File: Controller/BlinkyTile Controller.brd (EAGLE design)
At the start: 35 x 25 mm, 28 parts, among them CON1 USB_MICROSMT+THRUHULE, CON2 F-2X04-DIL-100, Q1 CRYSTAL_4PAD2520, SW1 SPST_TACT-EVQQ2, SW2 SPST_TACT-EVQQ2, U1 MK20D--VFM5, U2 W25Q80BV, U3 74LVC1G17DCK, U4 74LVC1G17DCK, U5 74LVC1G17DCK

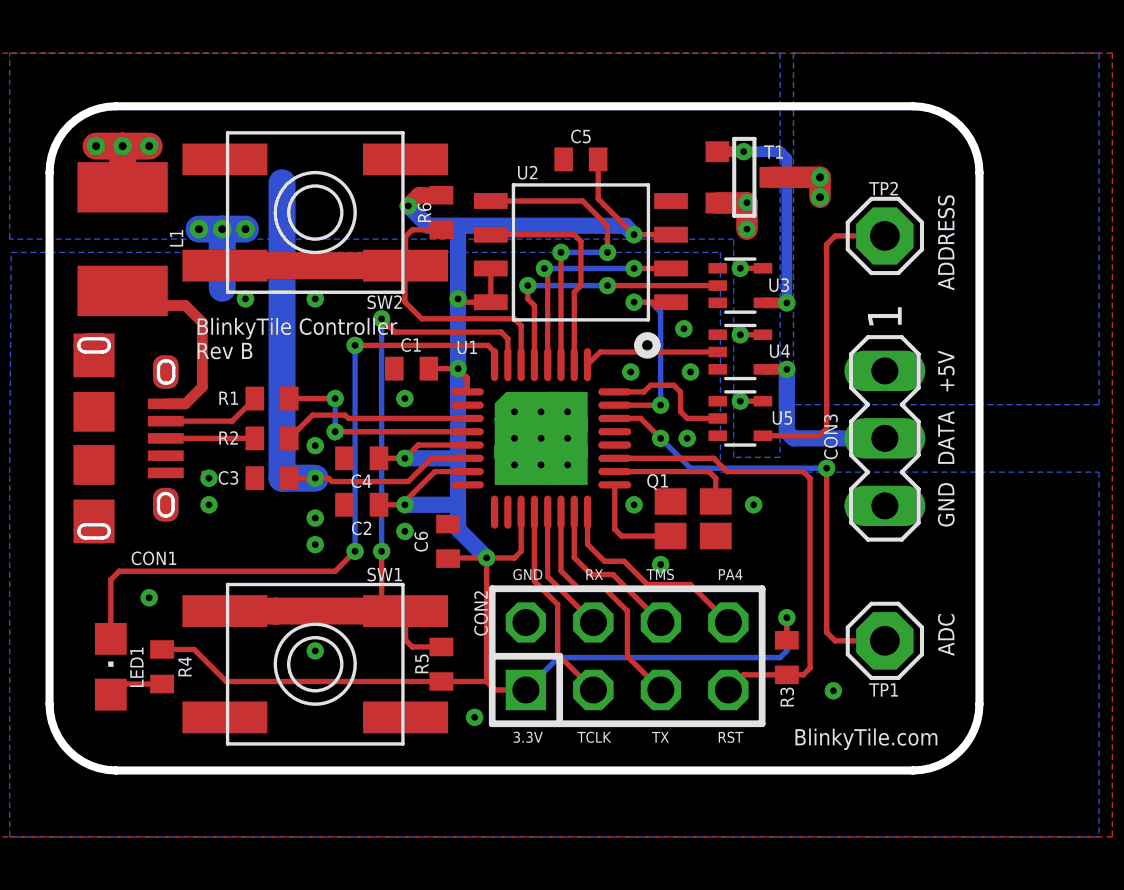
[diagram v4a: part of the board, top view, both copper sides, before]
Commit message: PCB updates: Drop pullup resistors, change connector
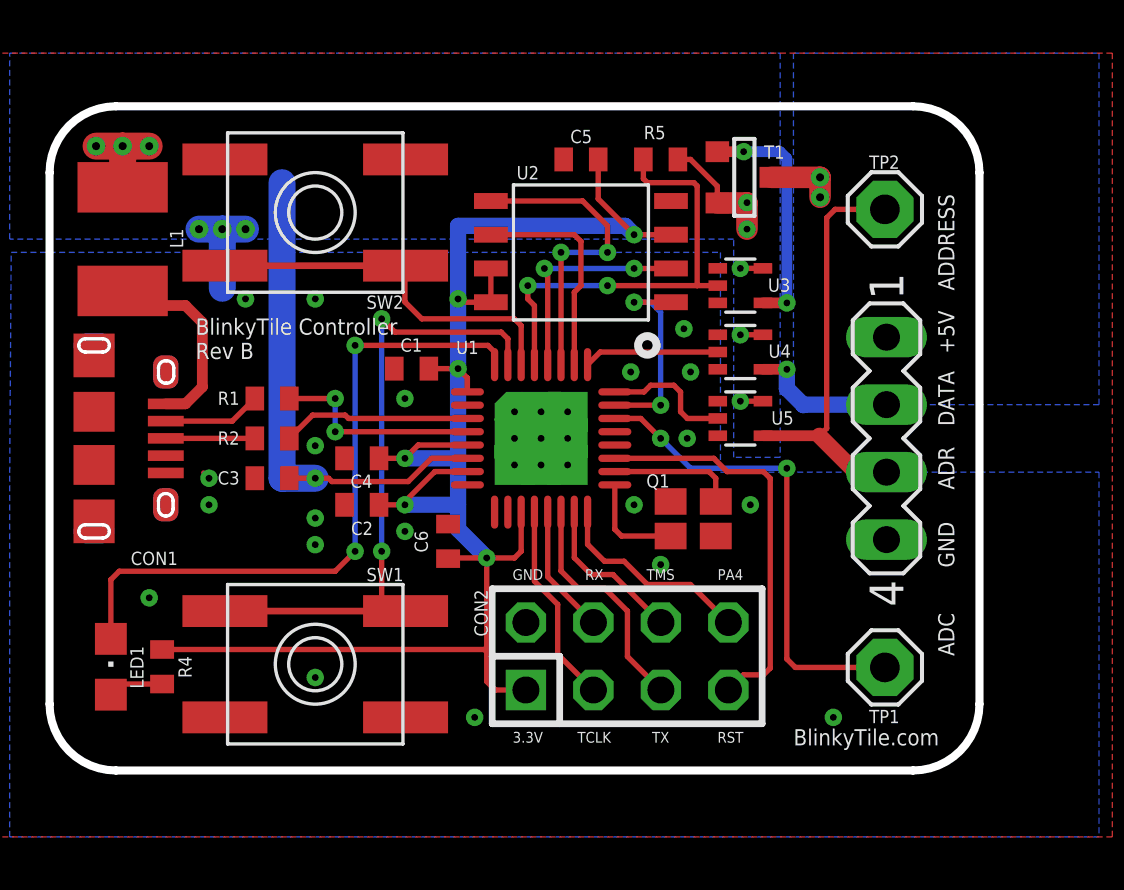
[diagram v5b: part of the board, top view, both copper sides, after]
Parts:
- removed CON3: (no value), con-lstb:MA03-1
- removed R3: 1k, adafruit:R0402
- removed R6: 10k, adafruit:R0402
- added SV1: (no value), con-lstb:MA04-1
- R4: value 1k -> 330
- R5: value 10k -> 1k
- moved R5 20.7 mm to (23.0, 10.5), turned to 0 degrees
- moved TP1 1.00 mm to (31.4, -8.62)
- moved TP2 1.00 mm to (31.4, 8.62)
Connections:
- net +3V3: no longer R3.2, R5.2, R6.2
- net +5V: now also R5.2
- net GND: now also SV1.4; no longer CON3.3
- net LED_DATA: now also SV1.2; no longer CON3.2
- net N$4: now also SV1.3
- net N$5: now also SV1.1; no longer CON3.1
- net POWER_ENABLE: now also R5.1
- net RESET: no longer R3.1
- net SW1: no longer R5.1
- net SW2: no longer R6.1
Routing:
- net +3V3: track 80.2 -> 63.6 mm, vias 8 -> 6
- net POWER_ENABLE: track 10.2 -> 16.8 mm
- net N$4: track 11.8 -> 15.9 mm
- net SW1: track 27.1 -> 23.8 mm
- net RESET: track 18.2 -> 15.2 mm
- net SW2: track 17.0 -> 14.4 mm
- net +5V: track 27.7 -> 30.2 mm
- net LED_DATA: track 7.04 -> 5.64 mm
- net ADC15: track 17.3 -> 18.3 mm
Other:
- board text added: "ADR"

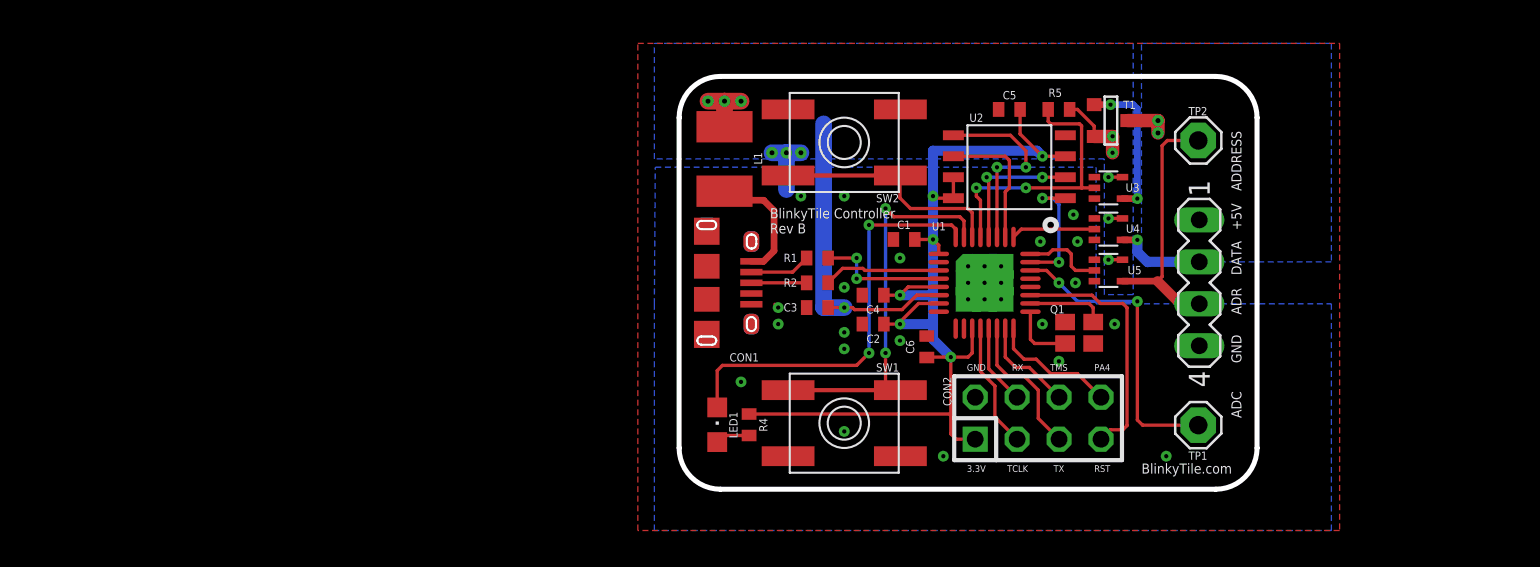
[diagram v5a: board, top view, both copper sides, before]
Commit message: Updated controller and panel designs
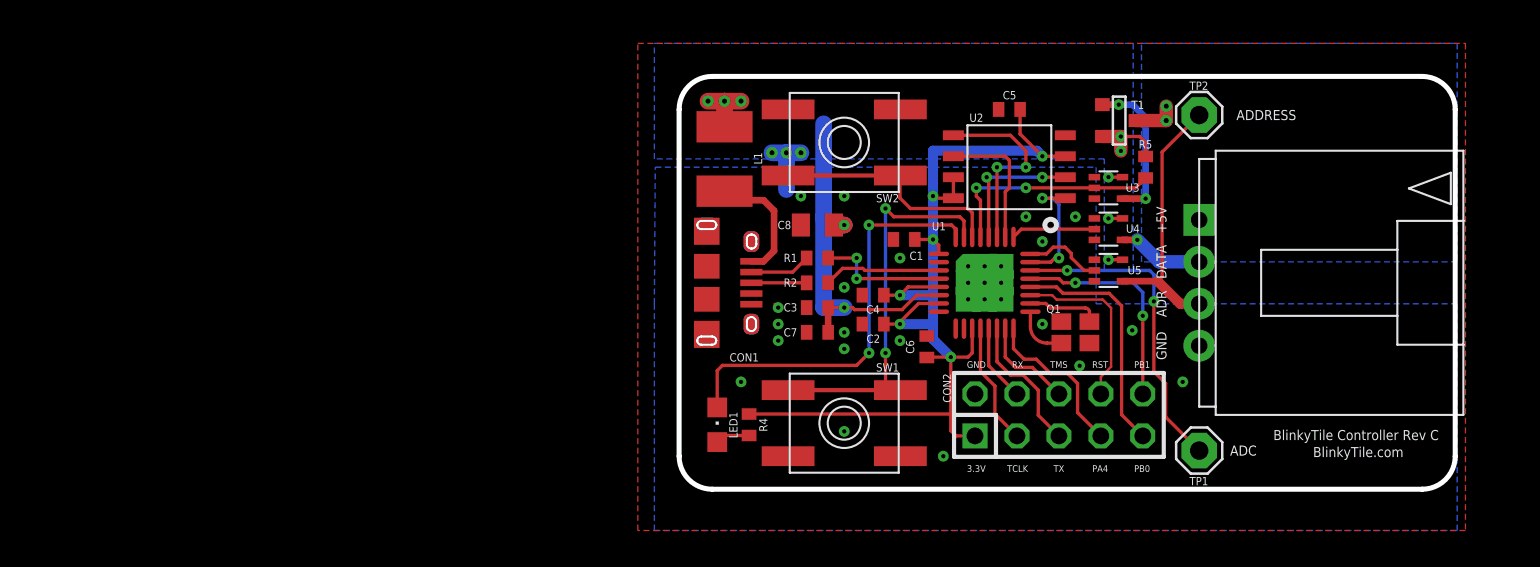
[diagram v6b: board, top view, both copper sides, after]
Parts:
- added C7: 100nF, adafruit:C0402
- added C8: 10uF, adafruit:C0805K
- CON2: value F-2X04-DIL-100 -> F-2X05-DIL-100; device con-headers-jp:DIL-100-2X04 -> con-headers-jp:DIL-100-2X05
- SV1: device con-lstb:MA04-1 -> dodocohedreled:4-PIN_DUPONT
- moved R5 6.31 mm to (28.2, 7.00), turned to 90 degrees
- moved TP1 1.54 mm to (31.5, -10.2)
- moved TP2 1.54 mm to (31.5, 10.2)
- moved CON2 1.28 mm to (23.0, -8.00)
- moved T1 0.50 mm to (26.6, 9.80)
- moved Q1 0.23 mm to (24.0, -3.00)
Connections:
- new net PB0: CON2.9, U1.20
- new net PB1: CON2.10, U1.21
- net +5V: now also C7.1, C8.1
- net GND: now also C7.2, C8.2, SV1.P$4; no longer SV1.4
- net LED_DATA: now also SV1.P$2; no longer SV1.2
- net N$4: now also SV1.P$3; no longer SV1.3
- net N$5: now also SV1.P$1; no longer SV1.1
- net PA4: now also CON2.7; no longer CON2.8
- net RESET: now also CON2.8; no longer CON2.7
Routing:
- net PB0: track 0.00 -> 14.4 mm
- net PB1: track 0.00 -> 13.3 mm, vias 0 -> 2
- net RESET: track 15.2 -> 10.7 mm
- net +5V: track 30.2 -> 33.7 mm, vias 9 -> 10
- net POWER_ENABLE: track 16.8 -> 13.6 mm
- net PA4: track 7.73 -> 9.73 mm
- net ADC15: track 18.3 -> 19.4 mm
- net N$2: track 3.88 -> 3.19 mm
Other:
- board size 35 x 25 mm -> 47 x 25 mm
- board text added: "BlinkyTile Controller Rev C"
- board text added: "PB0"
- board text added: "PB1"
- board text removed: "BlinkyTile Controller Rev B"

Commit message: Updated controller board, by Sam
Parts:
- removed C7: 100nF, adafruit:C0402
- turned U2 to 270 degrees
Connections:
- net +5V: no longer C7.1
- net GND: no longer C7.2
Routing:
- net FLASH_CS: track 7.62 -> 14.8 mm
- net FLASH_MOSI: track 11.8 -> 6.33 mm
- net +5V: track 33.7 -> 31.3 mm
- net FLASH_MISO: track 8.44 -> 6.43 mm, vias 2 -> 0
- net +3V3: track 63.4 -> 61.6 mm
- net FLASH_SCK: track 8.24 -> 6.73 mm
- net GND: vias 23 -> 24
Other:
- board size 47 x 25 mm -> 40 x 25 mm

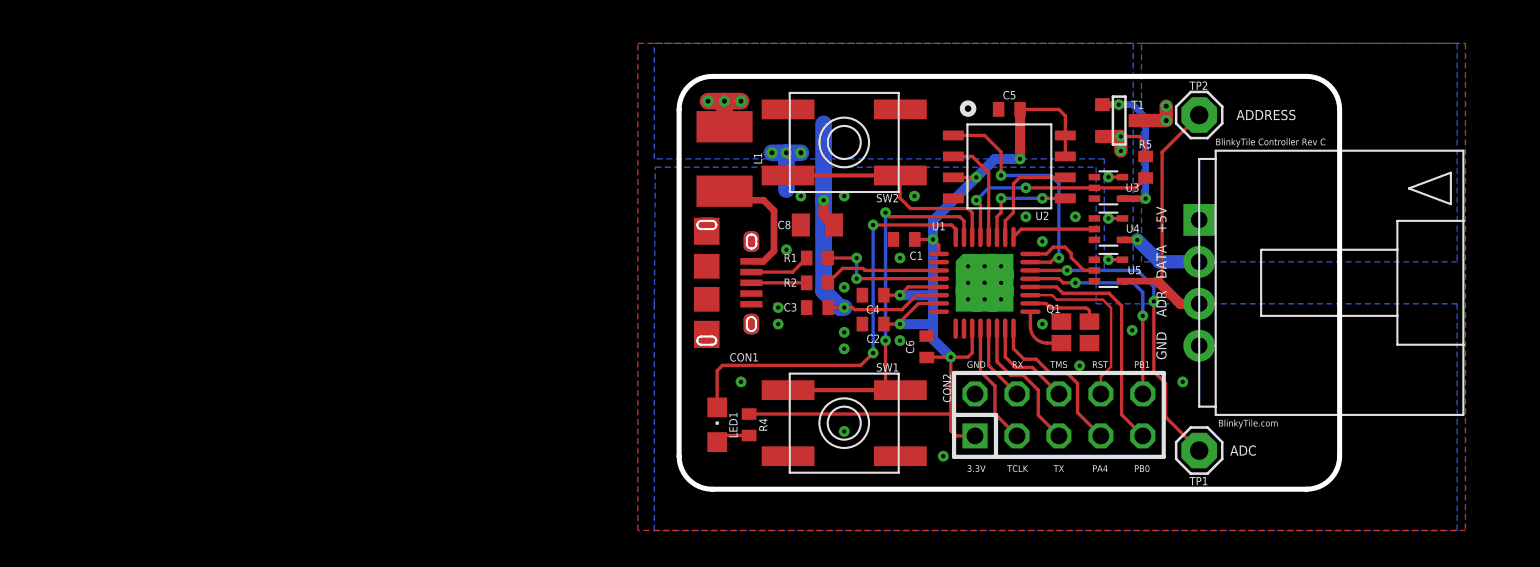
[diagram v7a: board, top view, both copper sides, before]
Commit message: Update controller: move R5 to 3.3v, reduce panel size, move more routing to top layer
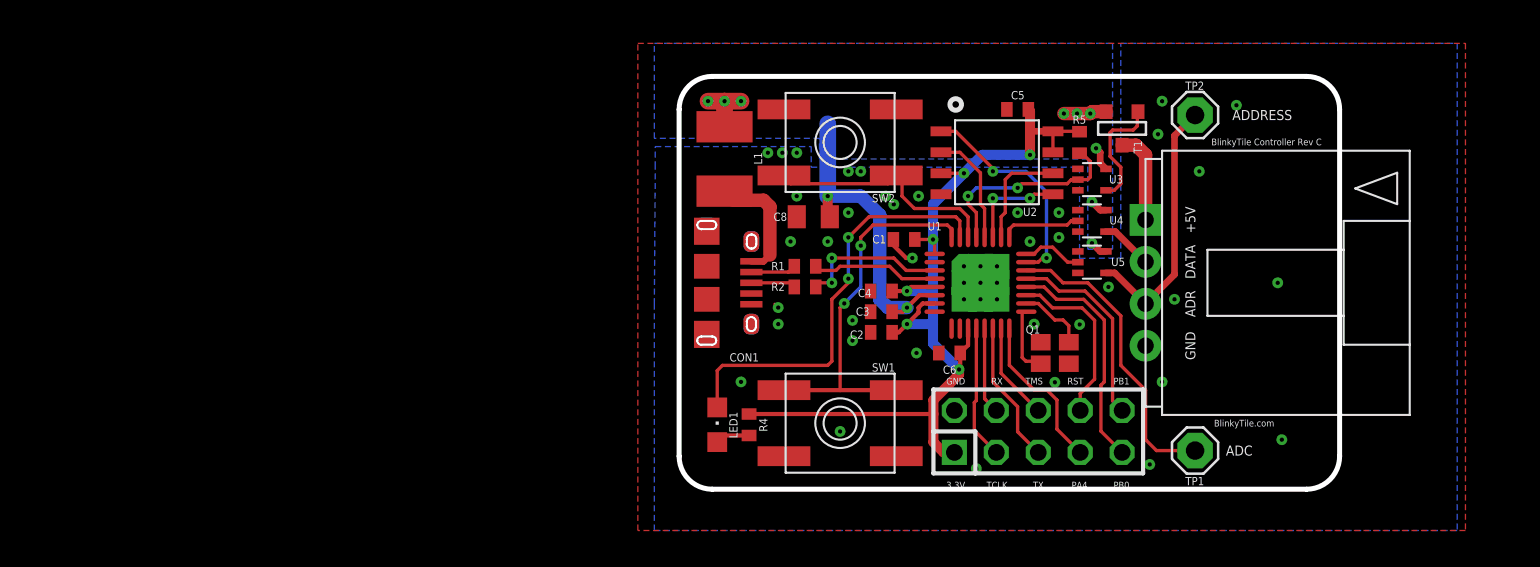
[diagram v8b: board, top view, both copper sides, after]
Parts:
- R5: value 1k -> 10k
- moved R5 4.27 mm to (24.2, 8.50)
- moved C3 3.88 mm to (12.2, -1.75)
- moved SV1 3.25 mm to (28.2, 0.00)
- moved Q1 1.77 mm to (22.8, -4.25)
- moved CON2 1.60 mm to (21.8, -9.00)
- moved C6 1.43 mm to (16.4, -4.25), turned to 180 degrees
- moved U3 1.12 mm to (25.0, 6.25)
- moved U4 1.12 mm to (25.0, 3.75)
- moved U5 1.12 mm to (25.0, 1.25)
- moved R1 0.90 mm to (7.62, 1.00)
- moved R2 0.79 mm to (7.62, -0.25)
- moved U2 0.79 mm to (19.2, 7.30)
- moved C2 0.71 mm to (12.2, -3.00)
- moved C4 0.56 mm to (12.2, -0.50)
- moved C8 0.56 mm to (8.12, 4.00)
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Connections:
- net +3V3: now also R5.2
- net +5V: no longer R5.2
- net STATUS: now also U1.31; no longer U1.32
- net SW1: now also U1.32; no longer U1.31
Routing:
- net +3V3: track 61.6 -> 58.3 mm
- net N$5: track 2.71 -> 5.61 mm, vias 2 -> 0
- net +5V: track 31.3 -> 29.0 mm, vias 10 -> 11
- net GND: track 4.26 -> 2.10 mm, vias 24 -> 38
- net N$6: track 9.26 -> 7.13 mm, vias 2 -> 0
- net LED_DATA: track 5.20 -> 3.15 mm, vias 1 -> 0
- net N$12: track 7.11 -> 9.11 mm, vias 0 -> 2
- net FLASH_CS: track 14.8 -> 13.3 mm
- net PB1: track 13.3 -> 12.0 mm, vias 2 -> 0
- net N$2: track 3.19 -> 4.31 mm
- net ADDRESS_PROGRAM: track 4.78 -> 3.67 mm
- net N$9: track 3.70 -> 2.74 mm
- net ADC15: track 18.9 -> 18.3 mm, vias 2 -> 0
- net TCLK: track 7.41 -> 8.10 mm
- net N$10: track 3.35 -> 2.70 mm
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- removed copper zone on layer 16, net N$5
